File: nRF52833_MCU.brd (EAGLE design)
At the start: 36.3 x 37.3 mm, 44 parts, among them IC1 SKY13415-485LF, J1 282834-2, J100 DEBUG_CONNECTOR, J2 282834-2, J3 282834-2, U1 nRF52833-QIAA, U3 BQ25570RGRR, X1 32MHz, X2 32.768kHz, X3 22-23-2031

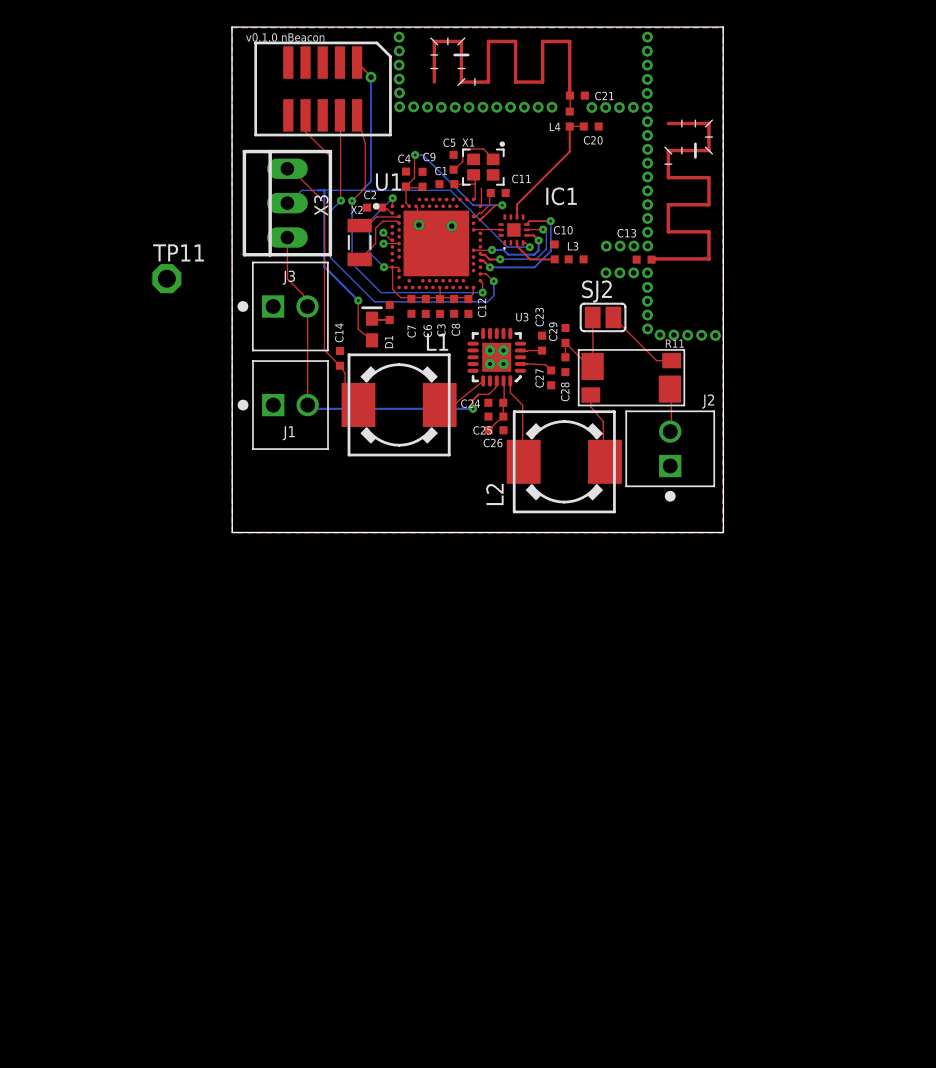
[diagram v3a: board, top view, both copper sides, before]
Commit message: Separate the power and the antennas
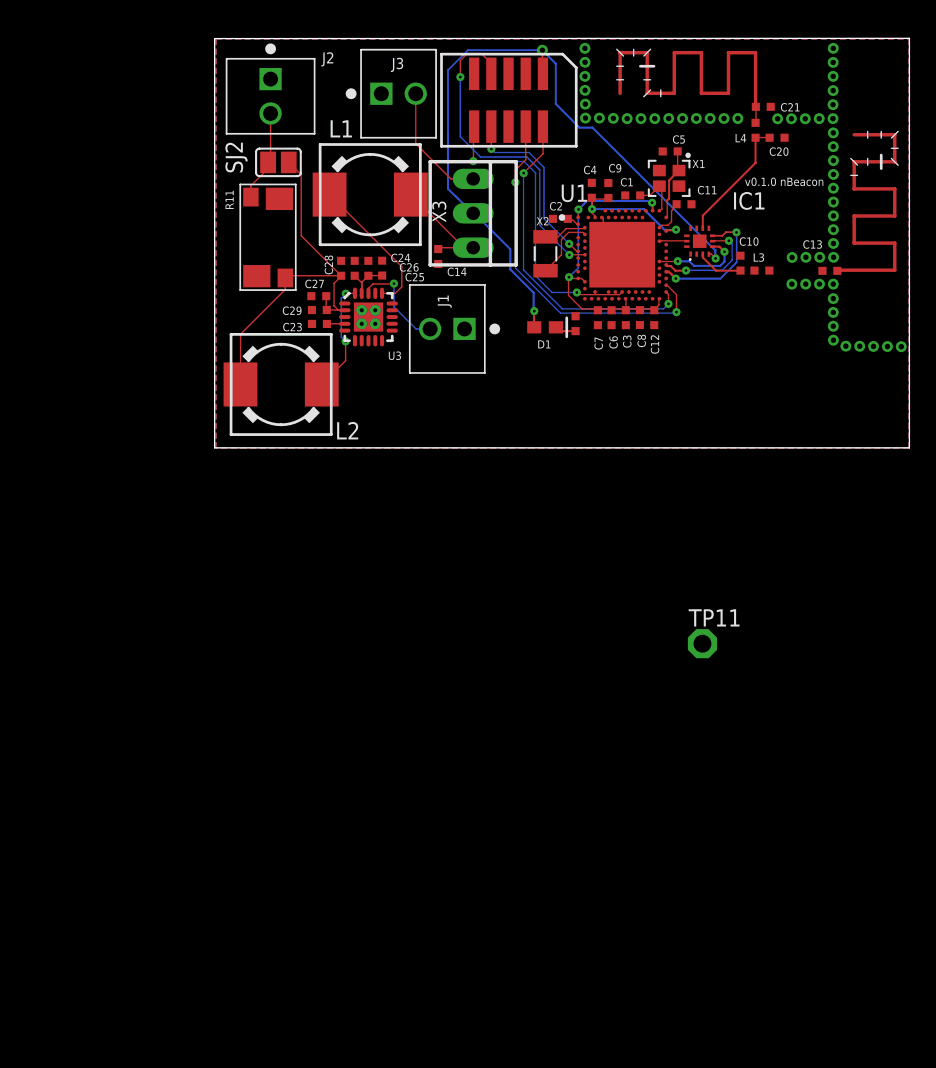
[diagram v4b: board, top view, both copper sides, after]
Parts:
- moved TP11 47.9 mm to (43.6, 22.3)
- moved J2 39.3 mm to (11.7, 62.8), turned to 270 degrees
- moved R11 28.7 mm to (11.6, 52.4), turned to 90 degrees
- moved SJ2 26.6 mm to (12.3, 57.9), turned to 180 degrees
- moved L2 21.7 mm to (12.5, 41.5), turned to 0 degrees
- moved C29 18.3 mm to (15.3, 47.0), turned to 180 degrees
- moved C27 18.2 mm to (15.3, 48.0), turned to 180 degrees
- moved C28 18.0 mm to (16.9, 50.1), turned to 90 degrees
- moved J3 17.6 mm to (21.2, 63.0)
- moved C23 16.5 mm to (15.3, 46.0), turned to 180 degrees
- moved C5 16.0 mm to (41.2, 58.7), turned to 180 degrees
- moved L1 15.7 mm to (19.1, 55.5), turned to 180 degrees
- moved C26 15.2 mm to (18.9, 50.1), turned to 90 degrees
- moved C24 14.4 mm to (17.9, 50.1), turned to 90 degrees
- moved C25 13.8 mm to (20.0, 50.1), turned to 90 degrees
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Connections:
- new net BQ_EXT_VBAT: J1.2, U3.18
- net EXT_VBAT: no longer J1.2, U3.18
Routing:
- net P0.07_RX: track 1.15 -> 26.2 mm, vias 1 -> 2
- net RESET: track 0.00 -> 22.2 mm, vias 0 -> 2
- net EXT_VBAT: track 28.6 -> 9.01 mm, vias 1 -> 0
- net BQ_VIN_DC: track 16.5 -> 28.7 mm
- net BQ_SUPPLY_VBAT: track 19.9 -> 8.85 mm
- net P0.06_TX: track 4.67 -> 14.6 mm, vias 1 -> 2
- net VDD_P3V3: track 44.2 -> 53.1 mm
- net BQ_EXT_VBAT: track 0.00 -> 7.46 mm, vias 0 -> 1
- net BQ_LBUCK: track 3.91 -> 10.7 mm
- net VDD: track 17.8 -> 23.9 mm, vias 2 -> 3
- net DEC6: track 15.6 -> 11.7 mm
- net BQ_RSP1: track 8.89 -> 6.78 mm
- net LBOOST: track 6.39 -> 8.39 mm, vias 0 -> 2
- net SWDIO: track 22.9 -> 24.2 mm
- net GND: track 0.71 -> 0.00 mm
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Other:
- board size 36.3 x 37.3 mm -> 51.3 x 30.2 mm

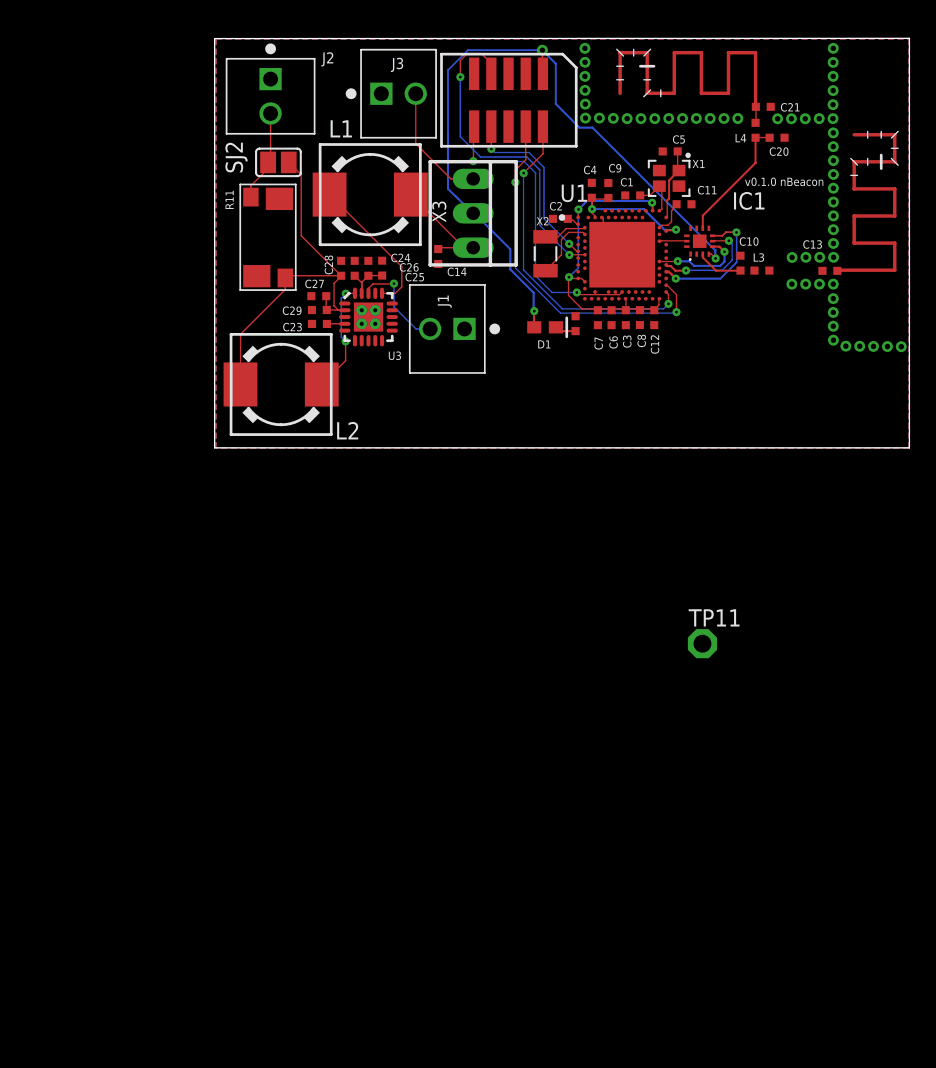
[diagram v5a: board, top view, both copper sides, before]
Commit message: Schematic: Move devices
Signed-off-by: Florian Depraz <florian.depraz@outlook.com>
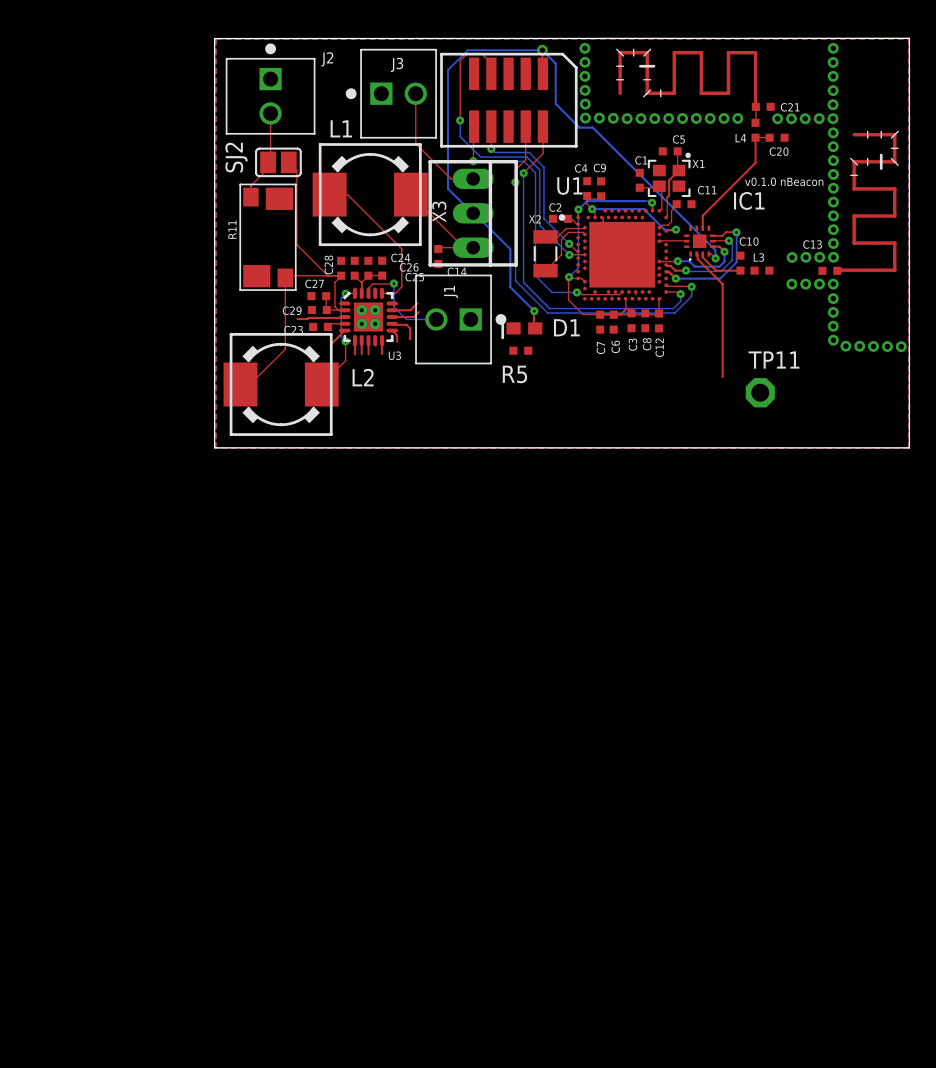
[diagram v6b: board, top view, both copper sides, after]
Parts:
- moved TP11 19.0 mm to (47.9, 40.9)
- moved R5 4.51 mm to (30.2, 44.0), turned to 180 degrees
- moved D1 1.53 mm to (30.5, 45.6), turned to 0 degrees
- moved C1 1.23 mm to (39.0, 56.6), turned to 90 degrees
- moved J1 0.84 mm to (25.2, 46.3)
- moved C9 0.56 mm to (36.1, 55.9)
- moved C3 0.48 mm to (38.4, 46.2)
- moved C8 0.47 mm to (39.4, 46.2)
- moved C12 0.42 mm to (40.4, 46.2)
- moved C7 0.37 mm to (36.1, 46.1)
- moved C6 0.37 mm to (37.1, 46.1)
- moved C4 0.36 mm to (35.1, 55.9)
- moved C23 0.23 mm to (15.4, 45.7)
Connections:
- net ANT renamed NRF_ANT
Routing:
- net ANT_OUT_RF3: track 0.00 -> 9.87 mm
- net VDD: track 23.9 -> 27.5 mm
- net VOC_SAMP: track 0.00 -> 3.56 mm
- net SWDCLK: track 26.5 -> 28.9 mm
- net BQ_VOUT_SET: track 0.00 -> 2.26 mm
- net SWDIO: track 24.2 -> 26.4 mm
- net BQ_VBAT_OK: track 0.00 -> 2.12 mm
- net BQ_VOUT: track 0.00 -> 2.09 mm
- net N$8: track 1.59 -> 0.00 mm
- net BQ_NEN: track 0.00 -> 1.42 mm
- net BQ_VOUT_EN: track 0.00 -> 1.02 mm
- net BQ_VRDIV: track 0.00 -> 1.00 mm
- net BQ_VBAT_OV: track 0.00 -> 0.99 mm
- net BQ_OK_HYST: track 0.00 -> 0.98 mm
- net BQ_OK_PROG: track 0.00 -> 0.97 mm
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
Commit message: Add the 5 antennas
Signed-off-by: Florian Depraz <florian.depraz@outlook.com>
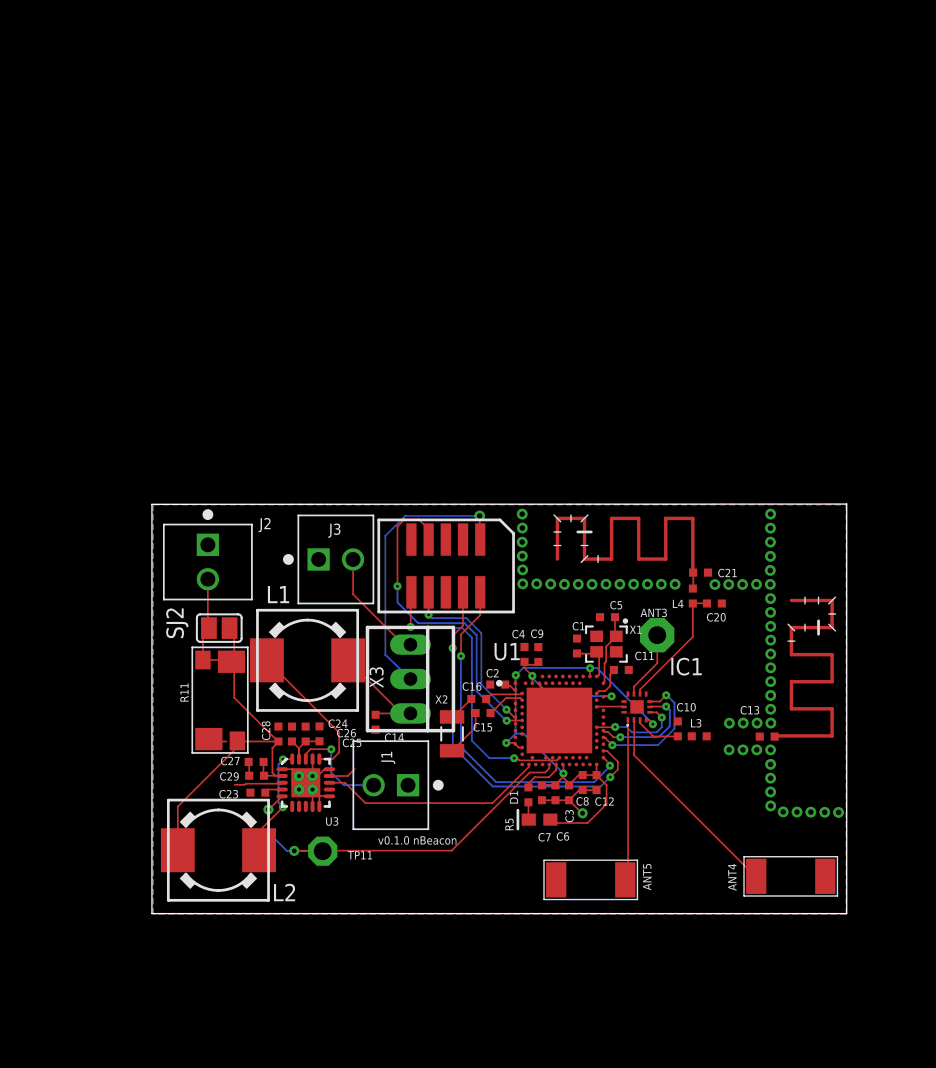
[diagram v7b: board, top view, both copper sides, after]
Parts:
- added ANT3: (no value), discrete:PAD-01
- added ANT4, ANT5: SWRA092B, texas:SWRA092B
- added C15, C16: 100nF, Nordic_misc:RESC0402_N
- moved TP11 46.8 mm to (15.6, 7.02)
- moved D1 36.3 mm to (31.6, 9.35)
- moved X2 36.1 mm to (25.1, 15.7)
- moved C3 35.2 mm to (33.8, 11.3)
- moved C6 35.0 mm to (32.8, 11.3)
- moved C7 35.0 mm to (31.8, 11.3)
- moved ANT1 34.7 mm to (49.2, 15.5)
- moved ANT2 34.7 mm to (42.9, 27.6)
- moved C1 34.7 mm to (34.4, 22.2)
- moved C10 34.7 mm to (41.8, 16.1)
- moved C11 34.7 mm to (37.6, 20.4)
- moved C13 34.7 mm to (48.4, 15.5)
- moved C14 34.7 mm to (19.5, 16.5)
- moved C2 34.7 mm to (28.5, 19.3)
- moved C20 34.7 mm to (44.5, 25.3)
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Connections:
- removed net BQ_OK_HYST: U3.10
- removed net BQ_OK_PROG: U3.11
- removed net GND: C1.2, C10.2, C11.2, C12.2, C13.2, C14.2, C2.2, C20.2, C21.2, C23.2, C24.2, C25.2, C26.2, C27.2, C28.2, C29.2, C4.2, C5.2, C6.2, C7.2, C8.2, C9.2, J1.1, J100.3, J100.5, J100.9, J2.1, J3.1, U3.1, U3.15, U3.17, U3.21, U3.22, U3.23, U3.24, U3.25, U3.9, X1.2, X1.4
- removed net P0.21_LED: R5.1, U1.AC17
- removed net VDD: C12.1, C3.1, C6.1, C7.1, C8.1, U1.A22, U1.AD14, U1.AD23, U1.B1, U1.W1, U1.Y2
- new net LED1: R5.1, U1.AD12
- new net N$2: C16.2, X2.1
- new net N$3: C15.2, X2.2
- net ANT_OUT_RF3: now also ANT4.1
- net ANT_OUT_RF4: now also ANT3.1
- net ANT_OUT_RF5: now also ANT5.1
- net BQ_NEN: now also TP11.TP, U1.AD10
- net BQ_VBAT_OK: now also U1.AD4
- net VDD_P3V3: now also C12.1, C3.1, C6.1, C7.1, C8.1, U1.A22, U1.AD14, U1.AD23, U1.B1, U1.W1, U1.Y2
- net VSS: now also C1.2, C10.2, C11.2, C12.2, C13.2, C14.2, C2.2, C20.2, C21.2, C23.2, C24.2, C25.2, C26.2, C27.2, C28.2, C29.2, C4.2, C5.2, C6.2, C7.2, C8.2, C9.2, J1.1, J100.3, J100.5, J100.9, J2.1, J3.1, U3.1, U3.10, U3.11, U3.15, U3.17, U3.21, U3.22, U3.23, U3.24, U3.25, U3.9, X1.2, X1.4
- net XL1: now also C16.1; no longer X2.1
- net XL2: now also C15.1; no longer X2.2
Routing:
- net BQ_NEN: track 1.42 -> 29.3 mm, vias 0 -> 2
- net VDD: track 27.5 -> 0.00 mm, vias 3 -> 0
- net VSS: track 5.06 -> 19.6 mm, vias 0 -> 1
- net BQ_VBAT_OK: track 2.12 -> 16.6 mm
- net ANT_OUT_RF5: track 0.00 -> 11.9 mm
- net VDD_P3V3: track 53.0 -> 61.4 mm, vias 3 -> 6
- net ANT_OUT_RF3: track 9.87 -> 15.3 mm
- net ANT_OUT_RF4: track 0.00 -> 5.07 mm
- net N$3: track 0.00 -> 3.51 mm
- net LED1: track 0.00 -> 3.16 mm
- net BQ_VOUT_SET: track 2.26 -> 0.10 mm
- net N$2: track 0.00 -> 1.97 mm
- net XL2: track 4.80 -> 3.10 mm
- net BQ_RSP1: track 6.78 -> 8.34 mm
- net N$8: track 0.00 -> 1.29 mm
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- added copper zone on layer 1, net VSS
- added copper zone on layer 16, net VSS
- removed copper zone on layer 1, net GND
- removed copper zone on layer 16, net GND

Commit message: Fix errors
Signed-off-by: Florian Depraz <florian.depraz@outlook.com>
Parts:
- moved R5 1.75 mm to (30.5, 9.45)
- moved D1 1.11 mm to (32.7, 9.15)
- moved C11 0.53 mm to (37.6, 19.9)
- moved R11 0.40 mm to (7.68, 18.2)
- moved ANT4 0.35 mm to (50.0, 4.85)
- moved C5 0.22 mm to (36.7, 24.1)
- moved J2 0.07 mm to (7.17, 28.4)
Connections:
- net VDD_P3V3 renamed VDD
- net VSS renamed GND
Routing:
- net VDD: track 61.4 -> 71.0 mm
- net GND: track 19.6 -> 15.0 mm, vias 1 -> 12
- net VOC_SAMP: track 3.56 -> 0.10 mm
- net BQ_VOUT: track 2.09 -> 0.00 mm
- net BQ_NEN: track 29.3 -> 31.0 mm
- net LED1: track 3.16 -> 4.90 mm
- net BQ_EXT_VBAT: track 7.64 -> 9.17 mm
- net RESET: track 22.2 -> 21.3 mm
- net DEC3: track 2.50 -> 1.90 mm
- net BQ_VIN_DC: track 29.4 -> 28.8 mm
